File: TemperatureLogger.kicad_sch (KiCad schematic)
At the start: 12 parts, among them J1 USB_A, SW1 RESET, SW2 A, SW3 B, SW4 MODE, U1 DHT11, U2 UA78M33_TO252, U3 ESP-12E, U4 TTL

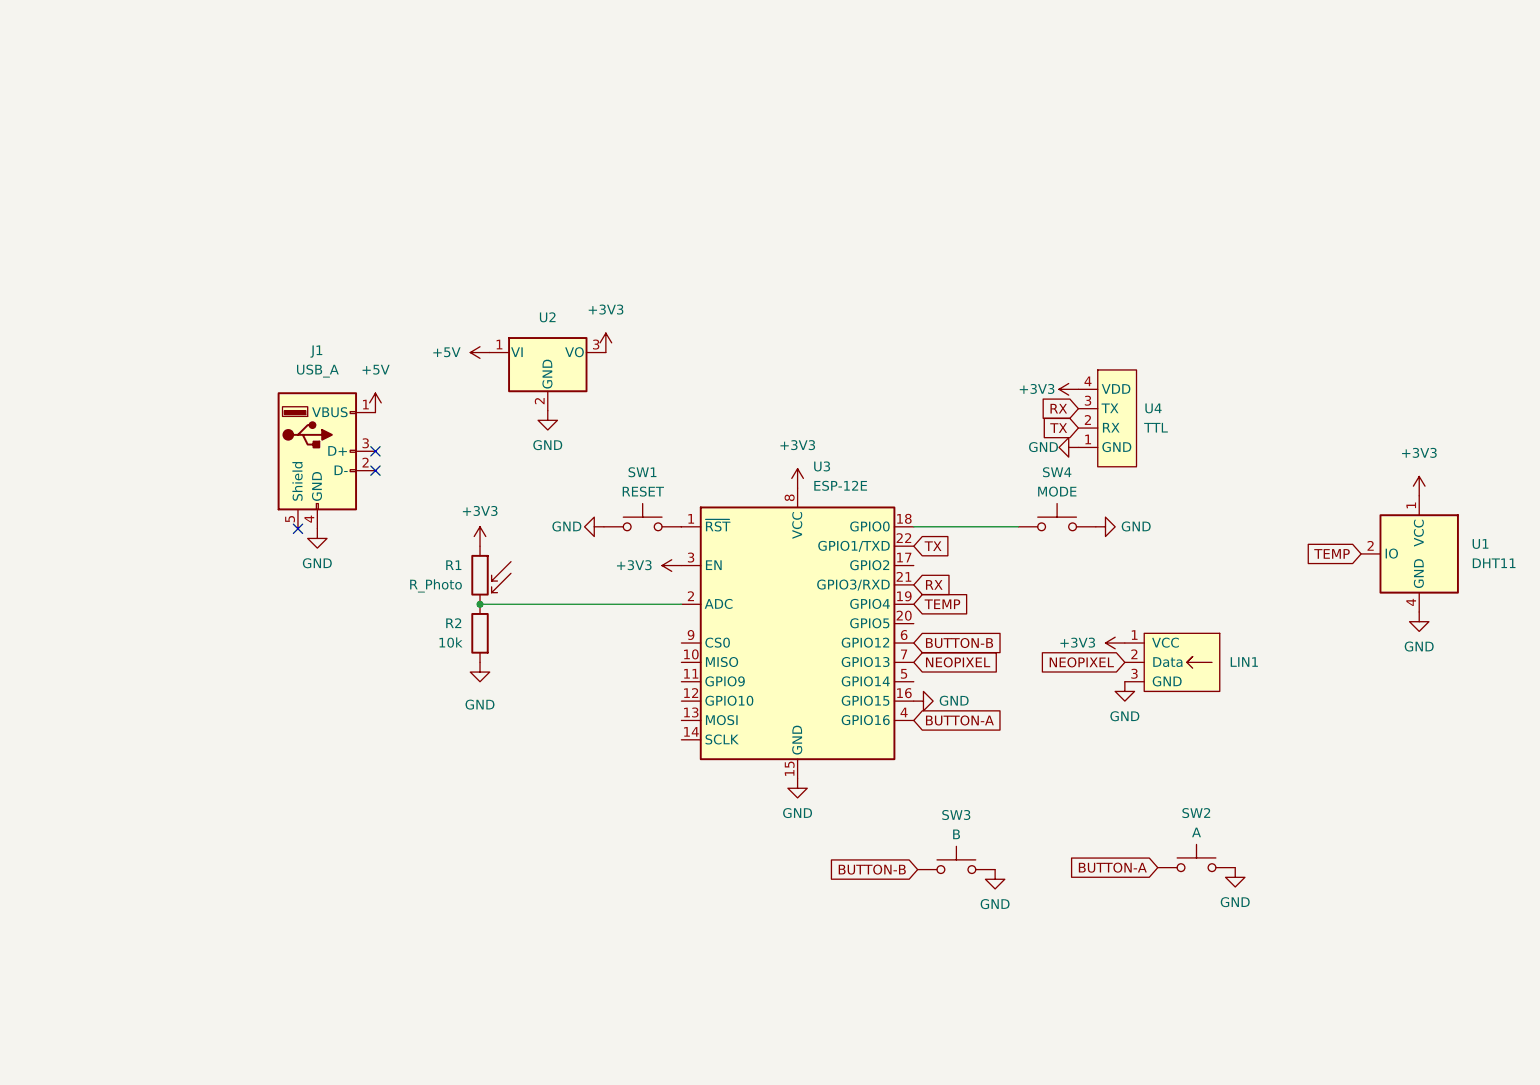
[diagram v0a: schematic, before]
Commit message: Add main components
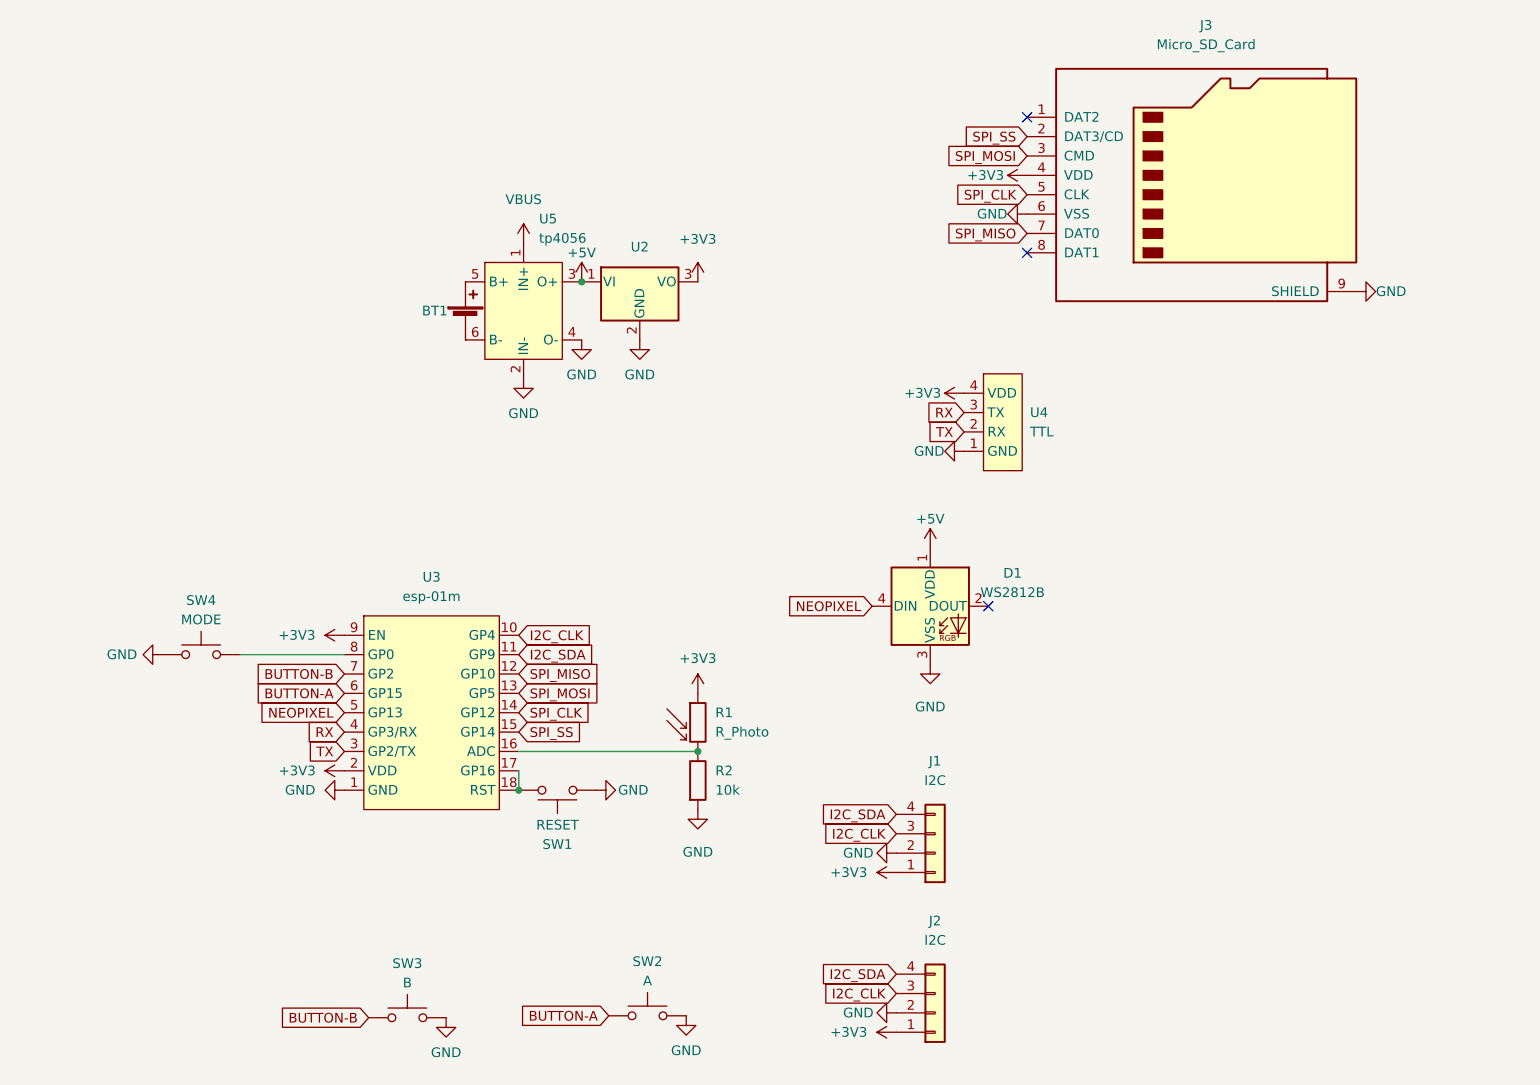
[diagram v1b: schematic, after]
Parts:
- removed J1: USB_A, usb-a-pcb:usb-a-pcb, symbol Connector:USB_A
- removed LIN1: LEDs_In, neopixel-strip:neopixel-strip, symbol neopixel-strip:LEDs_In
- removed U1: DHT11, Sensor:Aosong_DHT11_5.5x12.0_P2.54mm, symbol Sensor:DHT11
- removed U3: ESP-12E, RF_Module:ESP-12E, symbol RF_Module:ESP-12E
- added BT1: Battery_Cell, Connector_JST:JST_PH_B2B-PH-K_1x02_P2.00mm_Vertical, symbol Device:Battery_Cell
- added D1: WS2812B, LED_THT:LED_D5.0mm-4_RGB_Wide_Pins, symbol LED:WS2812B
- added J1, J2: I2C, Connector_PinHeader_2.54mm:PinHeader_1x04_P2.54mm_Vertical, symbol Connector_Generic:Conn_01x04
- added J3: Micro_SD_Card, sd-card:sd-card, symbol Connector:Micro_SD_Card
- added U3: esp-01m, esp-01m:esp-01m, symbol esp-01m:esp-01m
- added U5: tp4056, tp4056:tp4056, symbol tp4056:tp4056
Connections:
- net +3V3: now also J1.1 (Pin_1), J2.1 (Pin_1), J3.4 (VDD), U3.2 (VDD), U3.9 (EN)
- net +5V: now also D1.1 (VDD), U5.3 (O+)
- net BUTTON-A: now also U3.6 (GP15)
- net BUTTON-B: now also U3.7 (GP2)
- net GND: now also D1.3 (VSS), J1.2 (Pin_2), J2.2 (Pin_2), J3.6 (VSS), J3.9 (SHIELD), U3.1 (GND), U5.2 (IN-), U5.4 (O-)
- net NEOPIXEL: now also D1.4 (DIN), U3.5 (GP13)
- net RX: now also U3.4 (GP3/RX)
- net TX: now also U3.3 (GP2/TX)
- net at SW4.2: now also U3.8 (GP0)
- net at R1.2, R2.1: now also U3.16 (ADC)
- net at SW1.2: now also U3.17 (GP16), U3.18 (RST)
- new net: BT1.1 (+), U5.5 (B+)
- new net: BT1.2 (-), U5.6 (B-)
- new net I2C_CLK: J1.3 (Pin_3), J2.3 (Pin_3), U3.10 (GP4)
- new net I2C_SDA: J1.4 (Pin_4), J2.4 (Pin_4), U3.11 (GP9)
- new net SPI_CLK: J3.5 (CLK), U3.14 (GP12)
- new net SPI_MISO: J3.7 (DAT0), U3.12 (GP10)
- new net SPI_MOSI: J3.3 (CMD), U3.13 (GP5)
- new net SPI_SS: J3.2 (DAT3/CD), U3.15 (GP14)
- new net VBUS: U5.1 (IN+)
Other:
- title: ThumbLight -> TemperatureLogger
- moved on the sheet: R1, R2, SW1, SW2, SW3, SW4, U2, U4

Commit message: Add bme280 sensor and as12ap switch
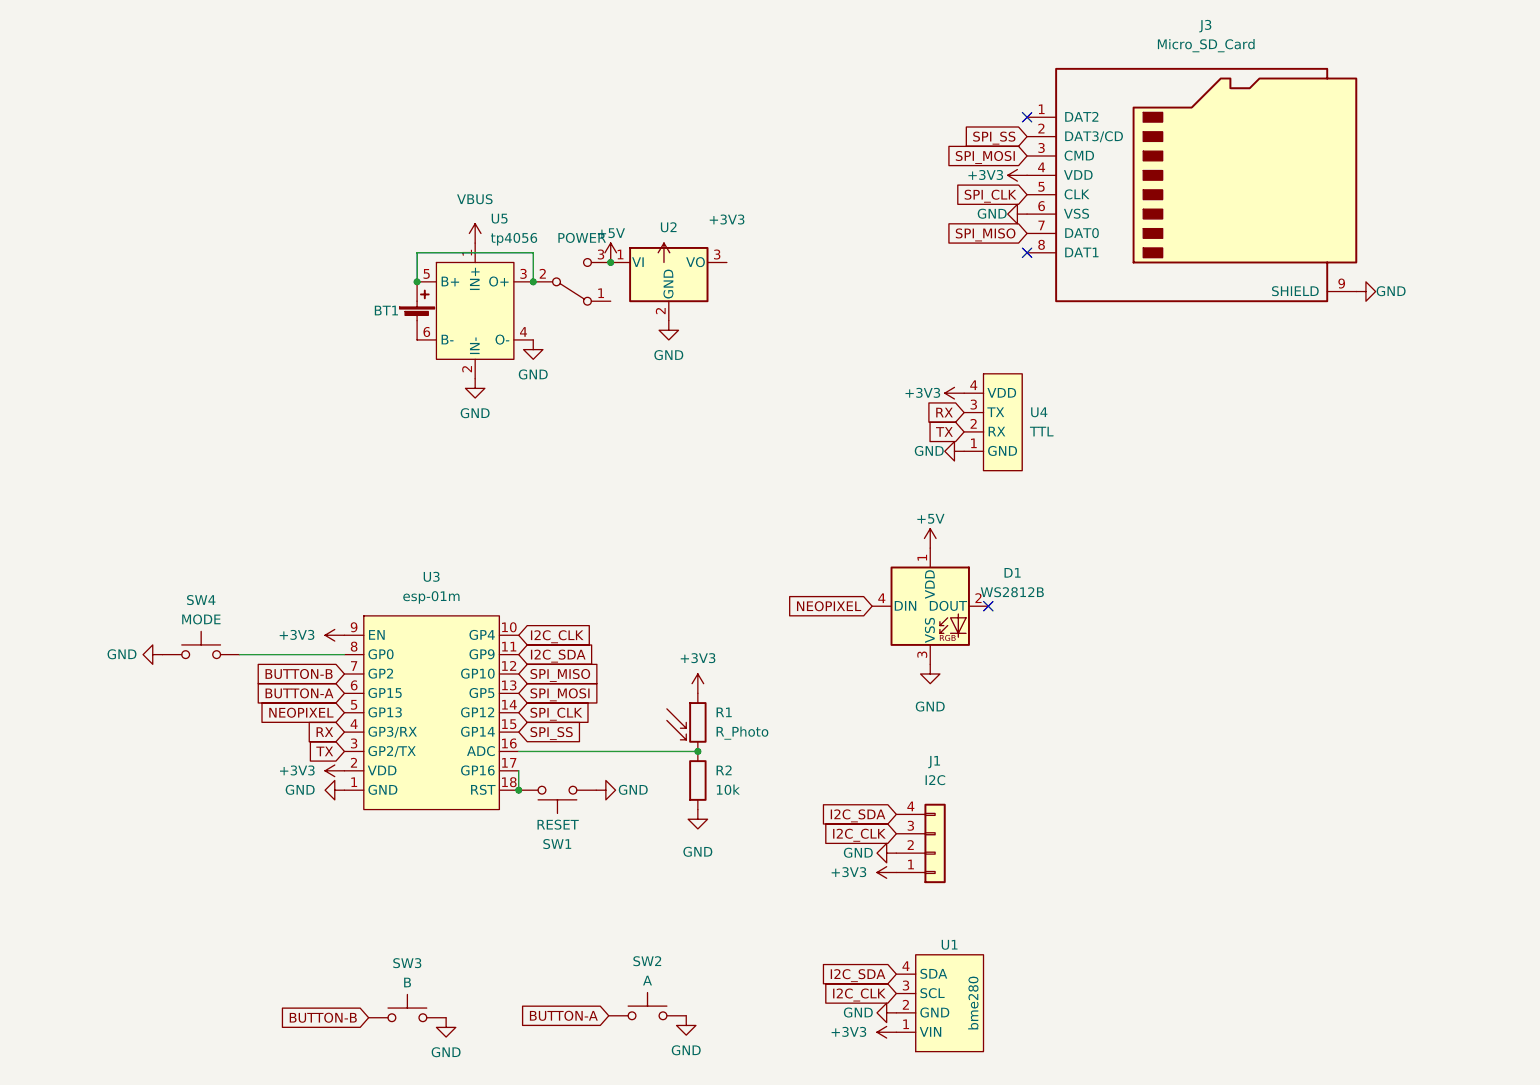
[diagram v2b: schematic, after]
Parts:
- removed J2: I2C, Connector_PinHeader_2.54mm:PinHeader_1x04_P2.54mm_Vertical, symbol Connector_Generic:Conn_01x04
- added SW5: POWER, as12ap:as12ap, symbol Switch:SW_SPDT
- added U1: bme280, bme280:bme280, symbol bme280:bme280
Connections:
- net +3V3: now also U1.1 (VIN); no longer U2.3 (VO)
- net +5V: now also SW5.3 (C); no longer U5.3 (O+)
- net GND: now also U1.2 (GND)
- net I2C_CLK: now also U1.3 (SCL)
- net I2C_SDA: now also U1.4 (SDA)
- net at BT1.1 (+), U5.5 (B+): now also U5.3 (O+), SW5.2 (B)
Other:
- moved on the sheet: BT1, U2, U5

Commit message: Update sd card module
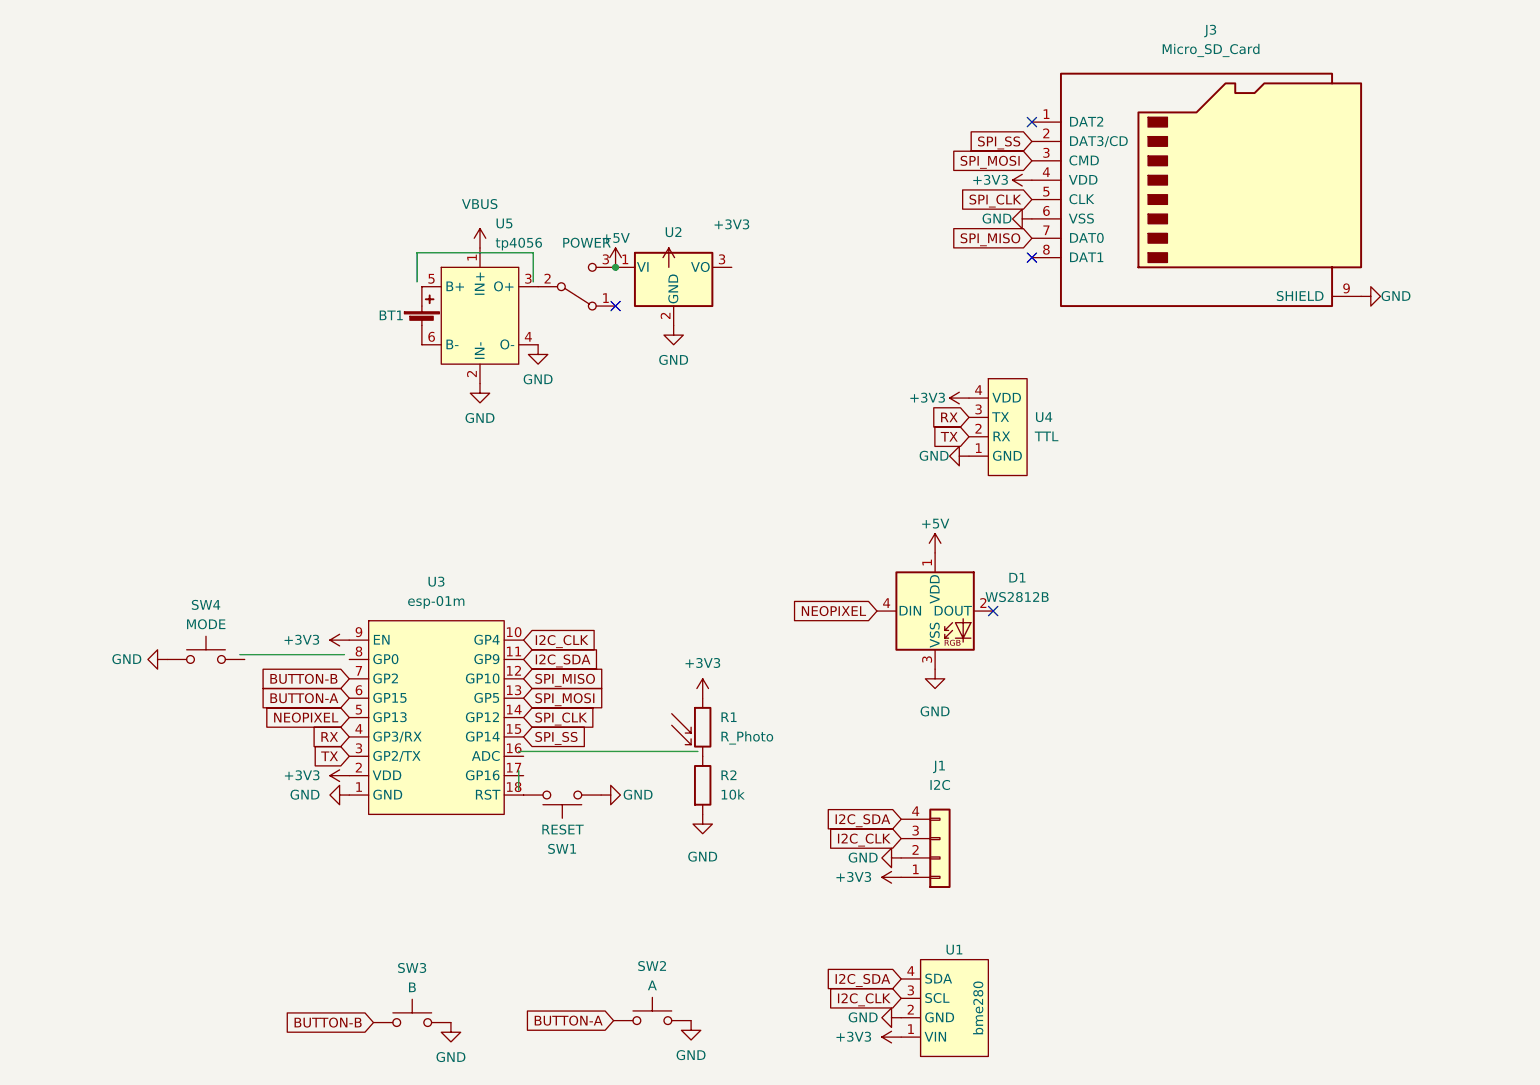
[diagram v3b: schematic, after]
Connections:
- net at SW4.2: no longer U3.8 (GP0)
- net at R1.2, R2.1: no longer U3.16 (ADC)
- net at SW5.2 (B), U5.3 (O+): no longer BT1.1 (+), U5.5 (B+)
- net at SW1.2, U3.18 (RST): no longer U3.17 (GP16)
- new net: BT1.1 (+), U5.5 (B+)
- no-connect marks 3 -> 4
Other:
- moved on the sheet: BT1, D1, J1, J3, R1, R2, SW1, SW2, SW3, SW4, U1, U2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

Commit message: First routing
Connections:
- net +3V3: now also U2.3 (VO)
- net VBUS: no longer U5.1 (IN+)
- net at SW4.2: now also U3.8 (GP0)
- net at R1.2, R2.1: now also U3.16 (ADC)
- net at SW5.2 (B), U5.3 (O+): now also BT1.1 (+), U5.5 (B+)
- net at U3.17 (GP16): now also SW1.2, U3.18 (RST)
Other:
- moved on the sheet: D1, J1, R1, R2, SW1, SW4, U1, U3, U4

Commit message: Addes todos
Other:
- note added: "TODO: Add 2x100uF Caps around the regulator Prepare for milling (holes etc.)"
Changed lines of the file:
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@@
     (stroke (width 0) (type default) (color 0 0 0 0))
+  )
+  (text "TODO:\n\nAdd 2x100uF Caps around the regulator\nPrepare for milling (holes etc.)"
+    (at 27.94 63.5 0)
+    (effects (font (size 1.27 1.27)) (justify left bottom))
   )
   (global_label "SPI_MISO" (shape input) (at 91.44 99.06 0) (fields_autoplaced)
